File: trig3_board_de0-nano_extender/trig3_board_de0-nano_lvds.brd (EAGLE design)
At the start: 233.2 x 160 mm, 75 parts, among them IC1 SN65LVDT388ADBT, IC2 SN65LVDT388ADBT, J12 4p-2.54, J131 4p-2.54, J14 BU-SMB-V, J19 6HE-160-VG64AC, J3 4p-2.54, J311 4p-2.54, J7 4p-2.54

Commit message: All major components
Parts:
- removed J7: 4p-2.54, Seeed-Connector:H4-2.54
- added C11, C12, C2, C4, C7, C9: 0.1uF, SparkFun-Capacitors:0805
- added IC3, IC4, IC5, IC6, IC7, IC8: SN65LVDT388ADBT, SamacSys_Parts:SOP50P640X120-38N
- added J4: 4p-2.54, Seeed-Connector:H4-2.54
- added JP3, JP4, JP5, JP6, JP7, JP8: 16, pinhead:2X08/90
- moved JP2 261.2 mm to (32.0, 109.0), flipped to the bottom
- moved IC2 224.1 mm to (31.0, 94.0), turned to 270 degrees
- moved C3 211.5 mm to (24.0, 92.0), turned to 90 degrees
- moved JP1 186.6 mm to (11.0, 109.0), flipped to the bottom, turned to 0 degrees
- moved IC1 165.7 mm to (10.0, 94.0), turned to 270 degrees
- moved C1 161.6 mm to (3.00, 92.0)
- moved LED1 106.4 mm to (-11.0, 96.0)
- moved R8 106.4 mm to (-5.00, 96.0)
- moved J311 96.2 mm to (-34.0, 94.0), turned to 270 degrees
- moved J3 84.0 mm to (-9.00, 106.0)
- moved J131 82.2 mm to (-23.0, 94.0), turned to 90 degrees
- moved B11 61.9 mm to (82.9, 69.0)
- moved B4 61.9 mm to (82.9, 49.0)
- moved E6 61.9 mm to (82.9, 8.95)
- moved N14 61.9 mm to (82.9, 28.9)
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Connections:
- new net N$100: IC6.8, JP6.7
- new net N$101: IC6.9, JP6.8
- new net N$102: IC6.11, JP6.9
- new net N$103: IC6.12, JP6.10
- new net N$104: IC6.13, JP6.11
- new net N$105: IC6.14, JP6.12
- new net N$106: IC6.16, JP6.13
- new net N$107: IC6.17, JP6.14
- new net N$108: IC6.18, JP6.15
- new net N$109: IC6.19, JP6.16
- new net N$110: C11.2, IC7.21, IC7.22, IC7.25, IC7.29, IC7.33, IC7.36, IC7.37
- new net N$111: C12.2, IC8.21, IC8.22, IC8.25, IC8.29, IC8.33, IC8.36, IC8.37
- new net N$112: IC7.1, JP7.1
- new net N$113: IC7.2, JP7.2
- new net N$114: IC7.3, JP7.3
- new net N$115: IC7.4, JP7.4
- new net N$116: IC7.6, JP7.5
- new net N$117: IC7.7, JP7.6
- new net N$118: IC7.8, JP7.7
- new net N$119: IC7.9, JP7.8
- new net N$120: IC7.11, JP7.9
- new net N$121: IC7.12, JP7.10
- new net N$122: IC7.13, JP7.11
- new net N$123: IC7.14, JP7.12
- new net N$124: IC7.16, JP7.13
- new net N$125: IC7.17, JP7.14
- new net N$126: IC7.18, JP7.15
- new net N$127: IC7.19, JP7.16
- new net N$128: IC8.1, JP8.1
- new net N$129: IC8.2, JP8.2
- new net N$130: IC8.3, JP8.3
- new net N$131: IC8.4, JP8.4
- new net N$132: IC8.6, JP8.5
- new net N$133: IC8.7, JP8.6
- new net N$134: IC8.8, JP8.7
- new net N$135: IC8.9, JP8.8
- new net N$136: IC8.11, JP8.9
- new net N$137: IC8.12, JP8.10
- new net N$138: IC8.13, JP8.11
- new net N$139: IC8.14, JP8.12
- new net N$140: IC8.16, JP8.13
- new net N$141: IC8.17, JP8.14
- new net N$142: IC8.18, JP8.15
- new net N$143: IC8.19, JP8.16
- new net N$42: C2.2, IC3.21, IC3.22, IC3.25, IC3.29, IC3.33, IC3.36, IC3.37
- new net N$43: C4.2, IC4.21, IC4.22, IC4.25, IC4.29, IC4.33, IC4.36, IC4.37
- new net N$44: IC3.1, JP3.1
- new net N$45: IC3.2, JP3.2
- new net N$46: IC3.3, JP3.3
- new net N$47: IC3.4, JP3.4
- new net N$48: IC3.6, JP3.5
- new net N$49: IC3.7, JP3.6
- new net N$50: IC3.8, JP3.7
- new net N$51: IC3.9, JP3.8
- new net N$52: IC3.11, JP3.9
- new net N$53: IC3.12, JP3.10
- new net N$54: IC3.13, JP3.11
- new net N$55: IC3.14, JP3.12
- new net N$56: IC3.16, JP3.13
- new net N$57: IC3.17, JP3.14
- new net N$58: IC3.18, JP3.15
- new net N$59: IC3.19, JP3.16
- new net N$60: IC4.1, JP4.1
- new net N$61: IC4.2, JP4.2
- new net N$62: IC4.3, JP4.3
- new net N$63: IC4.4, JP4.4
- new net N$64: IC4.6, JP4.5
- new net N$65: IC4.7, JP4.6
- new net N$66: IC4.8, JP4.7
- new net N$67: IC4.9, JP4.8
- new net N$68: IC4.11, JP4.9
- new net N$69: IC4.12, JP4.10
- new net N$70: IC4.13, JP4.11
- new net N$71: IC4.14, JP4.12
- new net N$72: IC4.16, JP4.13
- new net N$73: IC4.17, JP4.14
- new net N$74: IC4.18, JP4.15
- new net N$75: IC4.19, JP4.16
- new net N$76: C7.2, IC5.21, IC5.22, IC5.25, IC5.29, IC5.33, IC5.36, IC5.37
- new net N$77: C9.2, IC6.21, IC6.22, IC6.25, IC6.29, IC6.33, IC6.36, IC6.37
- new net N$78: IC5.1, JP5.1
- new net N$79: IC5.2, JP5.2
- new net N$80: IC5.3, JP5.3
- new net N$81: IC5.4, JP5.4
- new net N$82: IC5.6, JP5.5
- new net N$83: IC5.7, JP5.6
- new net N$84: IC5.8, JP5.7
- new net N$85: IC5.9, JP5.8
- new net N$86: IC5.11, JP5.9
- new net N$87: IC5.12, JP5.10
- new net N$88: IC5.13, JP5.11
- new net N$89: IC5.14, JP5.12
- new net N$90: IC5.16, JP5.13
- new net N$91: IC5.17, JP5.14
- new net N$92: IC5.18, JP5.15
- new net N$93: IC5.19, JP5.16
- new net N$94: IC6.1, JP6.1
- new net N$95: IC6.2, JP6.2
- new net N$96: IC6.3, JP6.3
- new net N$97: IC6.4, JP6.4
- new net N$98: IC6.6, JP6.5
- new net N$99: IC6.7, JP6.6
- net 5V: now also J3.2; no longer J7.4
- net GND: now also C11.1, C12.1, C2.1, C4.1, C7.1, C9.1, IC3.10, IC3.15, IC3.20, IC3.28, IC3.30, IC3.38, IC3.5, IC4.10, IC4.15, IC4.20, IC4.28, IC4.30, IC4.38, IC4.5, IC5.10, IC5.15, IC5.20, IC5.28, IC5.30, IC5.38, IC5.5, IC6.10, IC6.15, IC6.20, IC6.28, IC6.30, IC6.38, IC6.5, IC7.10, IC7.15, IC7.20, IC7.28, IC7.30, IC7.38, IC7.5, IC8.10, IC8.15, IC8.20, IC8.28, IC8.30, IC8.38, IC8.5, J3.1; no longer J7.3
- net GPIO_00_D3: now also IC3.31
- net GPIO_010_B6: now also IC7.27
- net GPIO_011_A6: now also IC7.26
- net GPIO_012_B7: now also IC3.32
- net GPIO_018_E7: now also IC6.23
- net GPIO_019_D8: now also J4.3
- net GPIO_01_C3: now also IC4.31
- net GPIO_021_F8: now also IC5.35
- net GPIO_022_F9: now also IC7.31
- net GPIO_023_E9: now also J4.2
- net GPIO_024_C9: now also IC4.26
- net GPIO_025_D9: now also IC4.27
- net GPIO_026_E11: now also IC6.27
- net GPIO_028_C11: now also IC7.34
- net GPIO_02_A2: now also IC3.26
- net GPIO_03_A3: now also IC3.27
- net GPIO_0_IN0_A8CLK: now also IC3.23
- net GPIO_0_IN1_B8CLK: now also IC3.24
- net GPIO_10_F13: now also IC6.34; no longer J3.2
- net GPIO_110_P11: now also IC6.26
- net GPIO_111_R10: now also IC3.34
- net GPIO_112_N12: now also J4.1
- net GPIO_113_P9: now also IC7.24
- net GPIO_115_N11: now also IC7.23
- net GPIO_120_P15: now also IC7.32
- net GPIO_126_L14: now also IC6.31; no longer J7.2
- net GPIO_129_L13: now also IC6.32; no longer J7.1
- net GPIO_12_T14: now also IC5.26
- net GPIO_132_J13: now also IC7.35
- net GPIO_14_R13: now also IC5.27
- net GPIO_15_T12: now also IC4.24
- net GPIO_16_R12: now also IC4.23
- net GPIO_18_T10: now also IC3.35
- net GPIO_19_R11: now also IC6.35; no longer J3.1
- net GPIO_1_IN0_T9CLK: now also IC5.23
- net GPIO_1_IN1_R9CLK: now also IC5.24
- net GPIO_20_A14: now also IC4.35
- net GPIO_210_F14: now also IC8.23
- net GPIO_211_G16: now also IC4.34
- net GPIO_212_G15: now also IC4.32
- net GPIO_21_B16: now also J4.4
- net GPIO_22_C14: now also IC8.26
- net GPIO_23_C16: now also IC6.24
- net GPIO_24_C15: now also IC8.27
- net GPIO_25_D16: now also IC8.35
- net GPIO_26_D15: now also IC8.24
- net GPIO_27_D14: now also IC8.34
- net GPIO_28_F15: now also IC8.32
- net GPIO_29_F16: now also IC8.31
- net GPIO_2_IN0_E15CLK: now also IC5.31
- net GPIO_2_IN1_E16CLK: now also IC5.32
- net GPIO_2_IN2_M16CLK: now also IC5.34
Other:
- board text added: "B16"
- board text added: "D8"
- board text added: "E9"
- board text added: "N12"
- board text removed: "F13"
- board text removed: "L13"
- board text removed: "L14"
- board text removed: "R11"

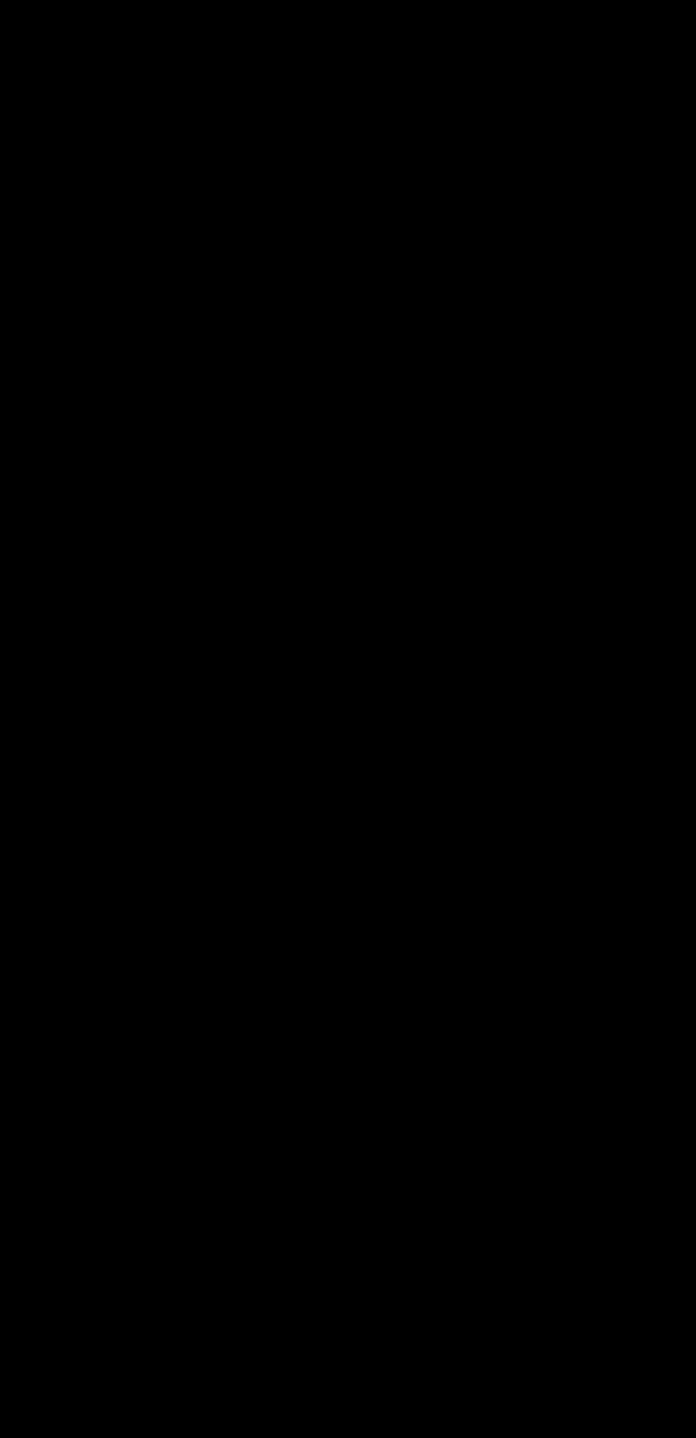
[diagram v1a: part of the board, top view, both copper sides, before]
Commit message: Added 3v3 supplies
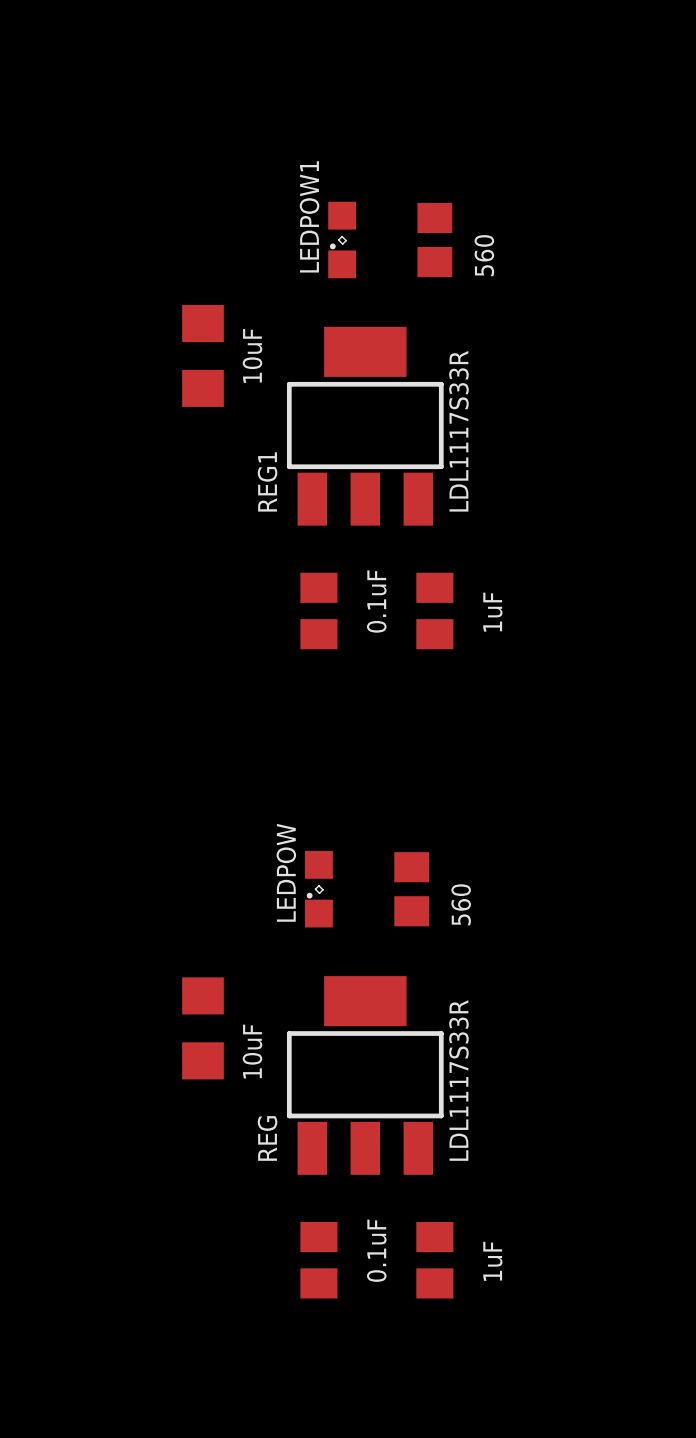
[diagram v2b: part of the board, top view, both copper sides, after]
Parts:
- added CP1, CP6: 10uF, rcl@1:C1206
- added CP11, CP4: 1uF, rcl:C0805K
- added CP2, CP3: 0.1uF, rcl:C0805K
- added LEDPOW, LEDPOW1: MF-LED-0805-RED, led:SML0805
- added REG, REG1: LDL1117S33R, Seeed-IC-2016:SOT-223
- added RLEDPOW, RLEDPOW1: 560, resistor:R0805
- J1, J2: value (none) -> 16
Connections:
- new net N$36: LEDPOW.C, RLEDPOW.1
- new net N$37: LEDPOW1.C, RLEDPOW1.1
- net 3V3: now also CP1.1, CP6.1, LEDPOW.A, LEDPOW1.A, REG.2, REG.TER, REG1.2, REG1.TER
- net 5V: now also CP11.2, CP2.1, CP3.1, CP4.2, REG.3, REG1.3
- net GND: now also CP1.2, CP11.1, CP2.2, CP3.2, CP4.1, CP6.2, REG.1, REG1.1, RLEDPOW.2, RLEDPOW1.2

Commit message: routed
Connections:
- removed net N$1: C1.2, IC1.21, IC1.22, IC1.25, IC1.29, IC1.33, IC1.36, IC1.37
- removed net N$110: C11.2, IC7.21, IC7.22, IC7.25, IC7.29, IC7.33, IC7.36, IC7.37
- removed net N$111: C12.2, IC8.21, IC8.22, IC8.25, IC8.29, IC8.33, IC8.36, IC8.37
- removed net N$3: C3.2, IC2.21, IC2.22, IC2.25, IC2.29, IC2.33, IC2.36, IC2.37
- removed net N$42: C2.2, IC3.21, IC3.22, IC3.25, IC3.29, IC3.33, IC3.36, IC3.37
- removed net N$43: C4.2, IC4.21, IC4.22, IC4.25, IC4.29, IC4.33, IC4.36, IC4.37
- removed net N$76: C7.2, IC5.21, IC5.22, IC5.25, IC5.29, IC5.33, IC5.36, IC5.37
- removed net N$77: C9.2, IC6.21, IC6.22, IC6.25, IC6.29, IC6.33, IC6.36, IC6.37
- net 3V3: now also C1.2, C11.2, C12.2, C2.2, C3.2, C4.2, C7.2, C9.2, IC1.21, IC1.22, IC1.25, IC1.29, IC1.33, IC1.36, IC1.37, IC2.21, IC2.22, IC2.25, IC2.29, IC2.33, IC2.36, IC2.37, IC3.21, IC3.22, IC3.25, IC3.29, IC3.33, IC3.36, IC3.37, IC4.21, IC4.22, IC4.25, IC4.29, IC4.33, IC4.36, IC4.37, IC5.21, IC5.22, IC5.25, IC5.29, IC5.33, IC5.36, IC5.37, IC6.21, IC6.22, IC6.25, IC6.29, IC6.33, IC6.36, IC6.37, IC7.21, IC7.22, IC7.25, IC7.29, IC7.33, IC7.36, IC7.37, IC8.21, IC8.22, IC8.25, IC8.29, IC8.33, IC8.36, IC8.37
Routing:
- net 3V3: track 0.00 -> 713.8 mm, vias 0 -> 5
- net GND: track 0.00 -> 349.9 mm, vias 0 -> 20
- net GPIO_114_N9: track 0.00 -> 290.0 mm, vias 0 -> 1
- net GPIO_113_P9: track 0.00 -> 264.7 mm, vias 0 -> 2
- net GPIO_24_C15: track 0.00 -> 242.8 mm, vias 0 -> 1
- net GPIO_210_F14: track 0.00 -> 219.8 mm, vias 0 -> 1
- net GPIO_26_D15: track 0.00 -> 213.2 mm, vias 0 -> 1
- net GPIO_27_D14: track 0.00 -> 207.3 mm, vias 0 -> 1
- net GPIO_29_F16: track 0.00 -> 201.3 mm, vias 0 -> 1
- net GPIO_023_E9: track 0.00 -> 189.6 mm
- net GPIO_115_N11: track 0.00 -> 188.6 mm, vias 0 -> 3
- net GPIO_28_F15: track 0.00 -> 188.0 mm, vias 0 -> 1
- net GPIO_10_F13: track 0.00 -> 183.1 mm, vias 0 -> 1
- net GPIO_22_C14: track 0.00 -> 179.5 mm, vias 0 -> 2
- net GPIO_21_B16: track 0.00 -> 176.2 mm, vias 0 -> 2
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
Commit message: routed with gnd on layers 2 and 15
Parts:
- SV1: value (none) -> 1
- SV2: value (none) -> 2
- moved J1 12.1 mm to (34.5, -4.50)
- moved J2 12.1 mm to (34.5, 8.60)
- moved R17 12.1 mm to (38.5, 67.1)
- moved SV1 12.1 mm to (41.0, 39.3)
- moved SV2 12.1 mm to (-2.30, 39.3)
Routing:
- net 5V: track 0.00 -> 753.9 mm, vias 0 -> 2
- net GPIO_126_L14: track 124.4 -> 341.0 mm, vias 2 -> 5
- net GPIO_120_P15: track 151.8 -> 334.4 mm, vias 2 -> 5
- net GPIO_114_N9: track 290.0 -> 444.9 mm, vias 1 -> 7
- net GPIO_211_G16: track 116.5 -> 256.9 mm, vias 2 -> 1
- net GND: track 349.9 -> 477.5 mm, vias 20 -> 89
- net GPIO_115_N11: track 188.6 -> 315.6 mm, vias 3 -> 5
- net GPIO_14_R13: track 121.9 -> 247.2 mm, vias 3 -> 5
- net GPIO_22_C14: track 179.5 -> 268.9 mm, vias 2 -> 3
- net GPIO_132_J13: track 148.3 -> 233.7 mm, vias 2 -> 5
- net GPIO_129_L13: track 128.6 -> 205.8 mm, vias 2 -> 5
- net GPIO_113_P9: track 264.7 -> 338.6 mm, vias 2 -> 5
- net GPIO_19_R11: track 135.1 -> 201.7 mm
- net GPIO_110_P11: track 128.7 -> 192.7 mm, vias 2 -> 7
- net AIN0: track 113.7 -> 170.4 mm, vias 0 -> 1
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- added copper zone on layer 15, net GND
- added copper zone on layer 2, net GND
- removed copper zone on layer 1, net 5V
- removed copper zone on layer 16, net GND

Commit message: try rj45 jack
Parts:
- removed JP1: 16, pinhead:2X08/90
- added J5, J6: RJ45, SparkFun-Connectors:RJ45-8
- moved J3 35.4 mm to (-34.0, 81.0)
- moved LED1 35.4 mm to (-36.0, 71.0)
- moved R8 35.4 mm to (-30.0, 71.0)
- moved C1 8.06 mm to (4.00, 84.0)
- moved C11 8.06 mm to (130.0, 84.0)
- moved C12 8.06 mm to (151.0, 84.0)
- moved C2 8.06 mm to (46.0, 84.0)
- moved C3 8.06 mm to (25.0, 84.0)
- moved C4 8.06 mm to (67.0, 84.0)
- moved C7 8.06 mm to (88.0, 84.0)
- moved C9 8.06 mm to (109.0, 84.0)
- moved IC1 8.06 mm to (11.0, 86.0)
- moved IC2 8.06 mm to (32.0, 86.0)
- moved IC3 8.06 mm to (53.0, 86.0)
- moved IC4 8.06 mm to (74.0, 86.0)
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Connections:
- removed net N$19: IC1.18, JP1.15
- removed net N$20: IC1.19, JP1.16
- new net N$1: IC1.1, J5.8
- new net N$3: IC1.3, J5.6
- net N$10: now also IC1.9, J5.1; no longer IC1.7, JP1.6
- net N$11: now also IC1.11, J6.8; no longer IC1.8, JP1.7
- net N$12: now also IC1.12, J6.7; no longer IC1.9, JP1.8
- net N$13: now also IC1.13, J6.6; no longer IC1.11, JP1.9
- net N$14: now also IC1.14, J6.3; no longer IC1.12, JP1.10
- net N$15: now also IC1.16, J6.5; no longer IC1.13, JP1.11
- net N$16: now also IC1.17, J6.4; no longer IC1.14, JP1.12
- net N$17: now also IC1.18, J6.2; no longer IC1.16, JP1.13
- net N$18: now also IC1.19, J6.1; no longer IC1.17, JP1.14
- net N$2: now also IC1.2, J5.7; no longer IC1.1, JP1.1
- net N$5: now also IC1.4, J5.3; no longer IC1.2, JP1.2
- net N$6: now also IC1.6, J5.5; no longer IC1.3, JP1.3
- net N$7: now also IC1.7, J5.4; no longer IC1.4, JP1.4
- net N$8: now also IC1.8, J5.2; no longer IC1.6, JP1.5
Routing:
- net GPIO_133_J14: track 168.0 -> 382.9 mm, vias 6 -> 3
- net GPIO_132_J13: track 233.7 -> 417.7 mm, vias 5 -> 4
- net GPIO_110_P11: track 192.7 -> 368.9 mm, vias 7 -> 5
- net GPIO_126_L14: track 341.0 -> 172.8 mm, vias 5 -> 3
- net GPIO_211_G16: track 256.9 -> 145.2 mm, vias 1 -> 4
- net GND: track 477.5 -> 382.2 mm, vias 89 -> 45
- net GPIO_114_N9: track 444.9 -> 355.1 mm, vias 7 -> 9
- net 3V3: track 707.3 -> 789.8 mm, vias 6 -> 15
- net GPIO_14_R13: track 247.2 -> 188.3 mm, vias 5 -> 6
- net 5V: track 753.9 -> 701.0 mm
- net AIN0: track 170.4 -> 118.4 mm, vias 1 -> 0
- net GPIO_021_F8: track 98.2 -> 147.5 mm, vias 3 -> 4
- net GPIO_032_D12: track 136.1 -> 176.9 mm, vias 6 -> 5
- net GPIO_10_F13: track 181.2 -> 219.3 mm, vias 4 -> 3
- net AIN2: track 158.8 -> 122.9 mm
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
